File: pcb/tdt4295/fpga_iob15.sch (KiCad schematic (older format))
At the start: 18 parts

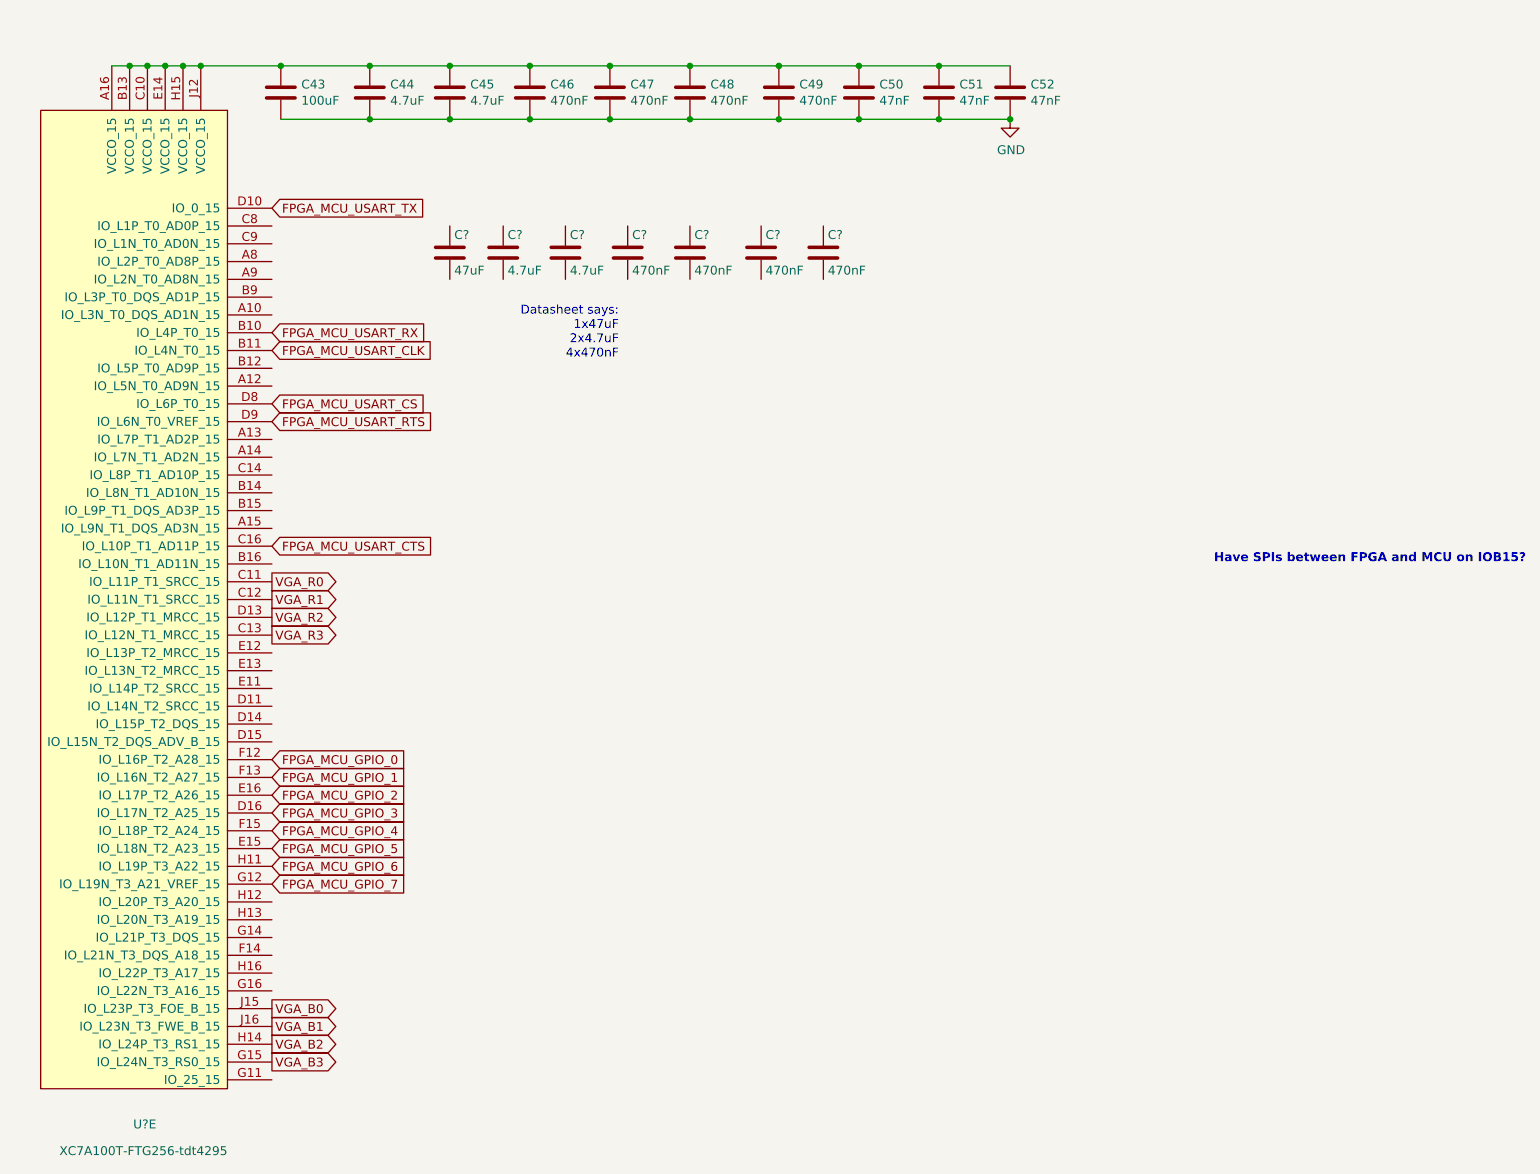
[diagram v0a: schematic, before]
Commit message: associate symbol components
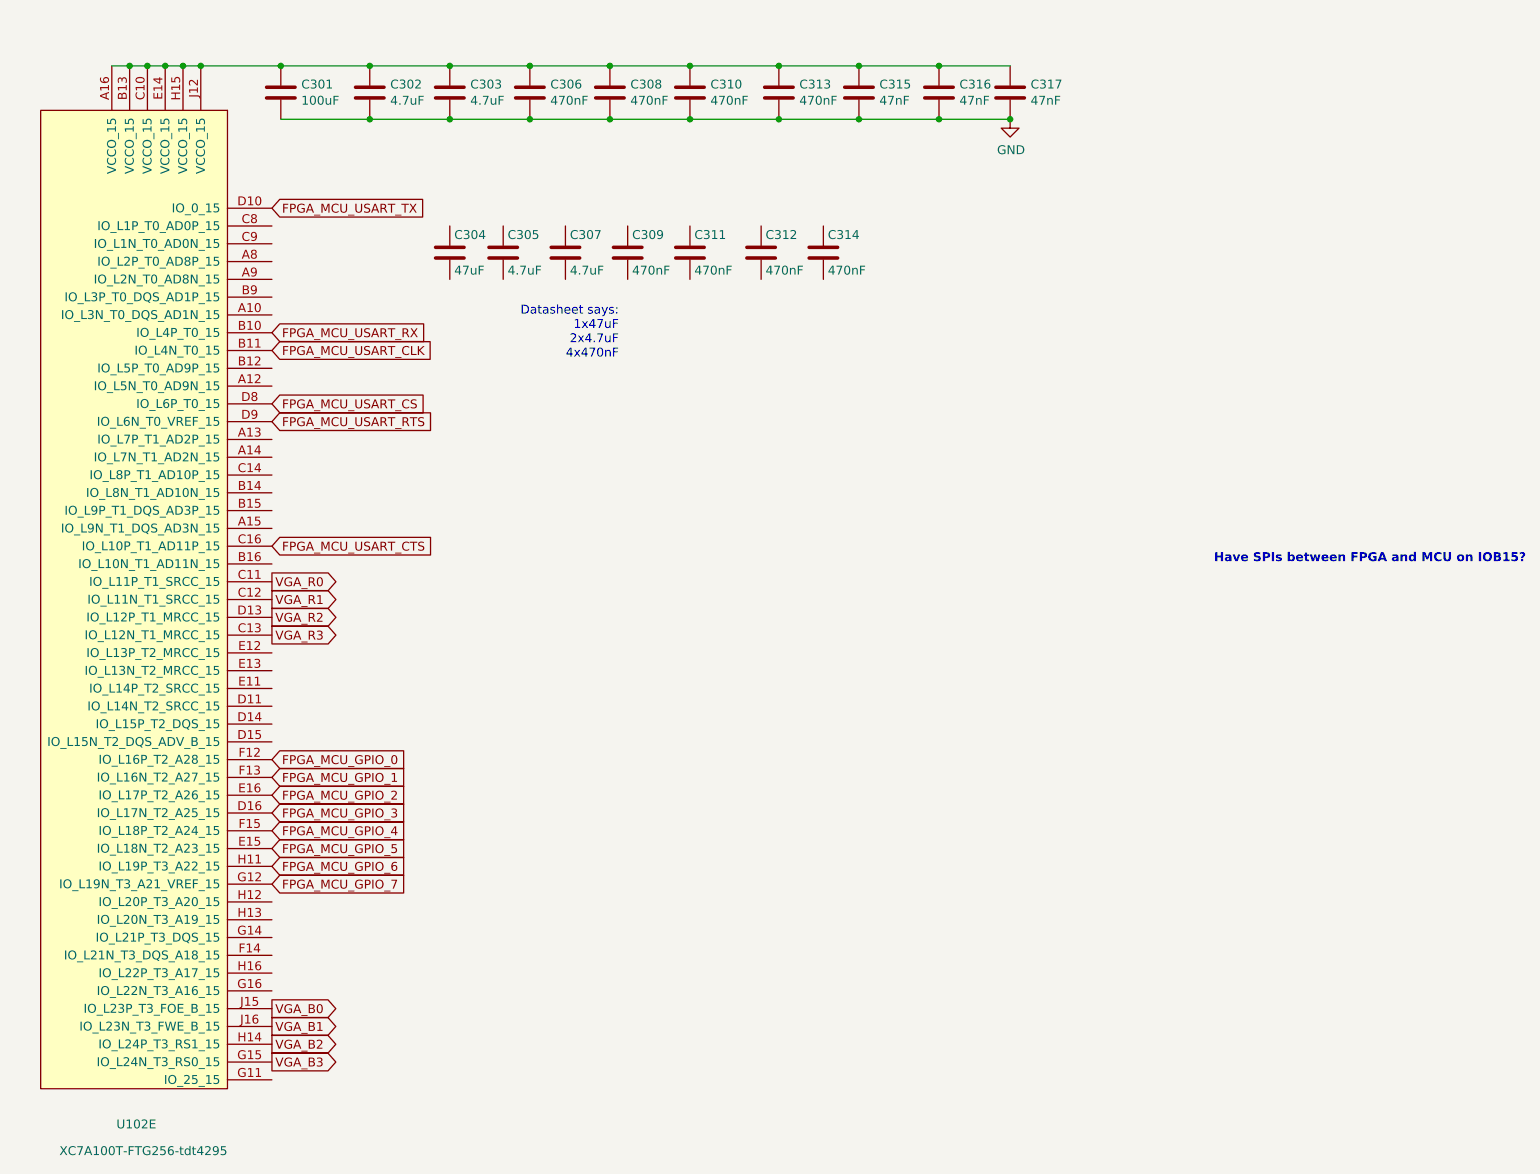
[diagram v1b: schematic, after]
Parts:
- U102: renamed from U?; footprint (none) -> Package_BGA:Xilinx_FTG256
- gave numbers to parts that had none: 7
- renumbered C43 to C301, C44 to C302, C45 to C303, C46 to C306, C47 to C308, C48 to C310, C49 to C313, C50 to C315, C51 to C316, C52 to C317
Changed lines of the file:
@@
 $EndDescr
 $Comp
-L xc7a100t-ftg256-modified:XC7A100T-FTG256-tdt4295 U?
+L xc7a100t-ftg256-modified:XC7A100T-FTG256-tdt4295 U102
 U 5 1 614C09B5
 P 1700 4050
-F 0 "U?" H 1700 1250 50  0000 R CNN
+F 0 "U102" H 1700 1250 50  0000 R CNN
 F 1 "XC7A100T-FTG256-tdt4295" H 2100 1100 50  0000 R CNN
-F 2 "" H 1700 1000 50  0001 C CNN
+F 2 "Package_BGA:Xilinx_FTG256" H 1700 1000 50  0001 C CNN
 F 3 "" H 1700 1000 50  0000 C CNN
 	5    1700 4050
@@
 $EndComp
 $Comp
-L Device:C C43
+L Device:C C301
 U 1 1 614DC8F2
 P 2400 1050
-F 0 "C43" H 2515 1096 50  0000 L CNN
+F 0 "C301" H 2515 1096 50  0000 L CNN
 F 1 "100uF" H 2515 1005 50  0000 L CNN
 F 2 "" H 2438 900 50  0001 C CNN
@@
 $EndComp
 $Comp
-L Device:C C44
+L Device:C C302
 U 1 1 614DE01C
 P 2900 1050
-F 0 "C44" H 3015 1096 50  0000 L CNN
+F 0 "C302" H 3015 1096 50  0000 L CNN
 F 1 "4.7uF" H 3015 1005 50  0000 L CNN
 F 2 "Capacitor_SMD:C_0805_2012Metric_Pad1.18x1.45mm_HandSolder" H 2938 900 50  0001 C CNN
@@
 $EndComp
 $Comp
-L Device:C C45
+L Device:C C303
 U 1 1 614DE58E
 P 3350 1050
-F 0 "C45" H 3465 1096 50  0000 L CNN
+F 0 "C303" H 3465 1096 50  0000 L CNN
 F 1 "4.7uF" H 3465 1005 50  0000 L CNN
 F 2 "Capacitor_SMD:C_0805_2012Metric_Pad1.18x1.45mm_HandSolder" H 3388 900 50  0001 C CNN
@@
 $EndComp
 $Comp
-L Device:C C46
+L Device:C C306
 U 1 1 614DEA18
 P 3800 1050
-F 0 "C46" H 3915 1096 50  0000 L CNN
+F 0 "C306" H 3915 1096 50  0000 L CNN
 F 1 "470nF" H 3915 1005 50  0000 L CNN
 F 2 "" H 3838 900 50  0001 C CNN
@@
 $EndComp
 $Comp
-L Device:C C47
+L Device:C C308
 U 1 1 614DF153
 P 4250 1050
-F 0 "C47" H 4365 1096 50  0000 L CNN
+F 0 "C308" H 4365 1096 50  0000 L CNN
 F 1 "470nF" H 4365 1005 50  0000 L CNN
 F 2 "" H 4288 900 50  0001 C CNN
@@
 $EndComp
 $Comp
-L Device:C C48
+L Device:C C310
 U 1 1 614DF5FE
 P 4700 1050
-F 0 "C48" H 4815 1096 50  0000 L CNN
+F 0 "C310" H 4815 1096 50  0000 L CNN
 F 1 "470nF" H 4815 1005 50  0000 L CNN
 F 2 "" H 4738 900 50  0001 C CNN
@@
 $EndComp
 $Comp
-L Device:C C49
+L Device:C C313
 U 1 1 614DFBD9
 P 5200 1050
-F 0 "C49" H 5315 1096 50  0000 L CNN
+F 0 "C313" H 5315 1096 50  0000 L CNN
 F 1 "470nF" H 5315 1005 50  0000 L CNN
 F 2 "Capacitor_SMD:C_0805_2012Metric_Pad1.18x1.45mm_HandSolder" H 5238 900 50  0001 C CNN
@@
 $EndComp
 $Comp
-L Device:C C50
+L Device:C C315
 U 1 1 614E00E6
 P 5650 1050
-F 0 "C50" H 5765 1096 50  0000 L CNN
+F 0 "C315" H 5765 1096 50  0000 L CNN
 F 1 "47nF" H 5765 1005 50  0000 L CNN
 F 2 "" H 5688 900 50  0001 C CNN
@@
 $EndComp
 $Comp
-L Device:C C51
+L Device:C C316
 U 1 1 614E08F1
 P 6100 1050
-F 0 "C51" H 6215 1096 50  0000 L CNN
+F 0 "C316" H 6215 1096 50  0000 L CNN
 F 1 "47nF" H 6215 1005 50  0000 L CNN
 F 2 "" H 6138 900 50  0001 C CNN
@@
 $EndComp
 $Comp
-L Device:C C52
+L Device:C C317
 U 1 1 614E0EB5
 P 6500 1050
-F 0 "C52" H 6615 1096 50  0000 L CNN
+F 0 "C317" H 6615 1096 50  0000 L CNN
 F 1 "47nF" H 6615 1005 50  0000 L CNN
 F 2 "" H 6538 900 50  0001 C CNN
@@
 	6100 1200 6500 1200
 $Comp
-L power:GND #PWR?
+L power:GND #PWR0301
 U 1 1 614E24A1
 P 6500 1200
-F 0 "#PWR?" H 6500 950 50  0001 C CNN
+F 0 "#PWR0301" H 6500 950 50  0001 C CNN
 F 1 "GND" H 6505 1027 50  0000 C CNN
 F 2 "" H 6500 1200 50  0001 C CNN
@@
 P 3350 1950
 AR Path="/61459CB7/615F1C9B" Ref="C?"  Part="1"
-AR Path="/614933B1/615F1C9B" Ref="C?"  Part="1"
-F 0 "C?" H 3375 2050 50  0000 L CNN
+AR Path="/614933B1/615F1C9B" Ref="C304"  Part="1"
+F 0 "C304" H 3375 2050 50  0000 L CNN
 F 1 "47uF" H 3375 1850 50  0000 L CNN
 F 2 "" H 3388 1800 50  0001 C CNN
@@
 P 3650 1950
 AR Path="/61459CB7/615F1CA1" Ref="C?"  Part="1"
-AR Path="/614933B1/615F1CA1" Ref="C?"  Part="1"
-F 0 "C?" H 3675 2050 50  0000 L CNN
+AR Path="/614933B1/615F1CA1" Ref="C305"  Part="1"
+F 0 "C305" H 3675 2050 50  0000 L CNN
 F 1 "4.7uF" H 3675 1850 50  0000 L CNN
 F 2 "Capacitor_SMD:C_0805_2012Metric_Pad1.18x1.45mm_HandSolder" H 3688 1800 50  0001 C CNN
@@
 P 4000 1950
 AR Path="/61459CB7/615F1CA7" Ref="C?"  Part="1"
-AR Path="/614933B1/615F1CA7" Ref="C?"  Part="1"
-F 0 "C?" H 4025 2050 50  0000 L CNN
+AR Path="/614933B1/615F1CA7" Ref="C307"  Part="1"
+F 0 "C307" H 4025 2050 50  0000 L CNN
 F 1 "4.7uF" H 4025 1850 50  0000 L CNN
 F 2 "Capacitor_SMD:C_0805_2012Metric_Pad1.18x1.45mm_HandSolder" H 4038 1800 50  0001 C CNN
@@
 P 4350 1950
 AR Path="/61459CB7/615F1CAD" Ref="C?"  Part="1"
-AR Path="/614933B1/615F1CAD" Ref="C?"  Part="1"
-F 0 "C?" H 4375 2050 50  0000 L CNN
+AR Path="/614933B1/615F1CAD" Ref="C309"  Part="1"
+F 0 "C309" H 4375 2050 50  0000 L CNN
 F 1 "470nF" H 4375 1850 50  0000 L CNN
 F 2 "" H 4388 1800 50  0001 C CNN
@@
 P 4700 1950
 AR Path="/61459CB7/615F1CB3" Ref="C?"  Part="1"
-AR Path="/614933B1/615F1CB3" Ref="C?"  Part="1"
-F 0 "C?" H 4725 2050 50  0000 L CNN
+AR Path="/614933B1/615F1CB3" Ref="C311"  Part="1"
+F 0 "C311" H 4725 2050 50  0000 L CNN
 F 1 "470nF" H 4725 1850 50  0000 L CNN
 F 2 "" H 4738 1800 50  0001 C CNN
@@
 P 5100 1950
 AR Path="/61459CB7/615F1CB9" Ref="C?"  Part="1"
-AR Path="/614933B1/615F1CB9" Ref="C?"  Part="1"
-F 0 "C?" H 5125 2050 50  0000 L CNN
+AR Path="/614933B1/615F1CB9" Ref="C312"  Part="1"
+F 0 "C312" H 5125 2050 50  0000 L CNN
 F 1 "470nF" H 5125 1850 50  0000 L CNN
 F 2 "" H 5138 1800 50  0001 C CNN
@@
 P 5450 1950
 AR Path="/61459CB7/615F1CBF" Ref="C?"  Part="1"
-AR Path="/614933B1/615F1CBF" Ref="C?"  Part="1"
-F 0 "C?" H 5475 2050 50  0000 L CNN
+AR Path="/614933B1/615F1CBF" Ref="C314"  Part="1"
+F 0 "C314" H 5475 2050 50  0000 L CNN
 F 1 "470nF" H 5475 1850 50  0000 L CNN
 F 2 "" H 5488 1800 50  0001 C CNN

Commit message: Major restructuring of FPGA outputs
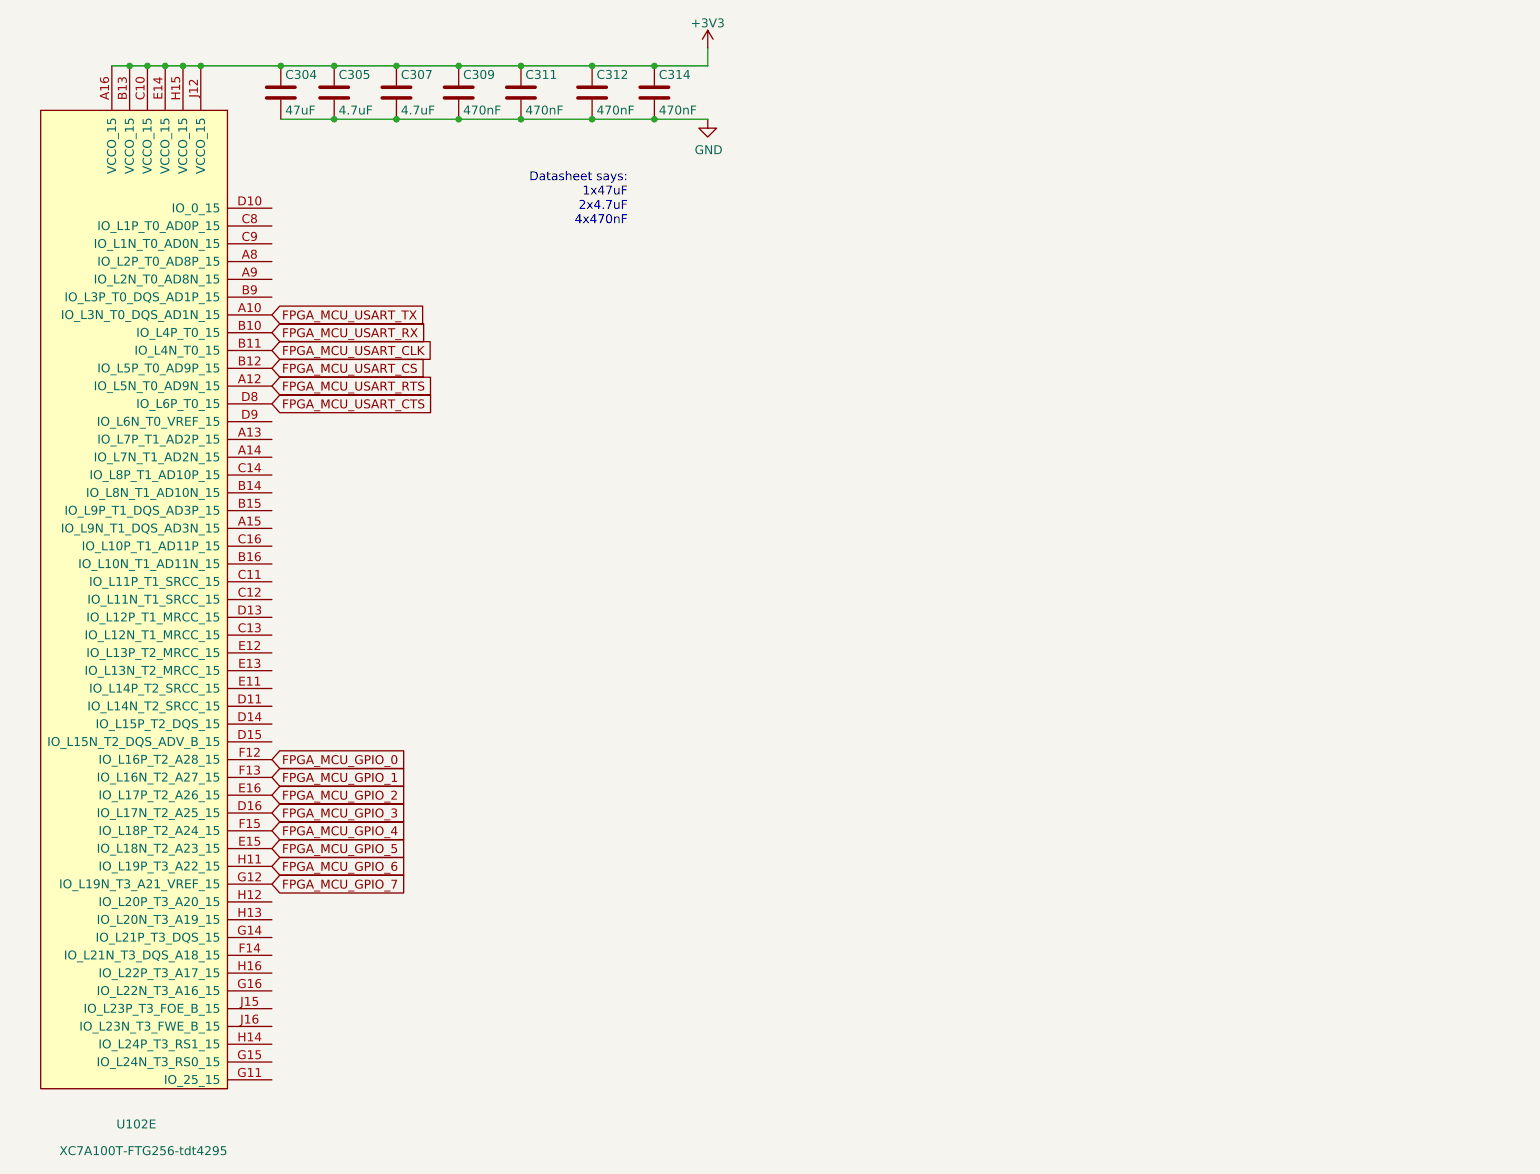
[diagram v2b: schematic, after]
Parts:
- removed C301: 100uF, symbol Device:C
- removed C302, C303: 4.7uF, Capacitor_SMD:C_0805_2012Metric_Pad1.18x1.45mm_HandSolder, symbol Device:C
- removed C306, C308, C310: 470nF, symbol Device:C
- removed C313: 470nF, Capacitor_SMD:C_0805_2012Metric_Pad1.18x1.45mm_HandSolder, symbol Device:C
- removed C315, C316, C317: 47nF, symbol Device:C
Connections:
- net FPGA_MCU_USART_CS: now also U102.B12 (IO_L5P_T0_AD9P_15); no longer U102.D8 (IO_L6P_T0_15)
- net FPGA_MCU_USART_CTS: now also U102.D8 (IO_L6P_T0_15); no longer U102.C16 (IO_L10P_T1_AD11P_15)
- net FPGA_MCU_USART_RTS: now also U102.A12 (IO_L5N_T0_AD9N_15); no longer U102.D9 (IO_L6N_T0_VREF_15)
- net FPGA_MCU_USART_TX: now also U102.A10 (IO_L3N_T0_DQS_AD1N_15); no longer U102.D10 (IO_0_15)
- net GND: now also C304.2, C305.2, C307.2, C309.2, C311.2, C312.2, C314.2
- net +3V3: now reaches U102.A16 (VCCO_15), U102.B13 (VCCO_15), U102.C10 (VCCO_15), U102.E14 (VCCO_15), U102.H15 (VCCO_15), U102.J12 (VCCO_15)
- net +3V3: now also C304.1, C305.1, C307.1, C309.1, C311.1, C312.1, C314.1
- net VGA_B0: no longer names the net of U102.J15 (IO_L23P_T3_FOE_B_15)
- net VGA_B1: no longer names the net of U102.J16 (IO_L23N_T3_FWE_B_15)
- net VGA_B2: no longer names the net of U102.H14 (IO_L24P_T3_RS1_15)
- net VGA_B3: no longer names the net of U102.G15 (IO_L24N_T3_RS0_15)
- net VGA_R0: no longer names the net of U102.C11 (IO_L11P_T1_SRCC_15)
- net VGA_R1: no longer names the net of U102.C12 (IO_L11N_T1_SRCC_15)
- net VGA_R2: no longer names the net of U102.D13 (IO_L12P_T1_MRCC_15)
- net VGA_R3: no longer names the net of U102.C13 (IO_L12N_T1_MRCC_15)
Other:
- note removed: "Have SPIs between FPGA and MCU on IOB15?"
- moved on the sheet: C304, C305, C307, C309, C311, C312, C314
